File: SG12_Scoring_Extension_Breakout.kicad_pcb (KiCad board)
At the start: 2 copper layers, 95 x 49 mm, 24 parts, among them J1 RJ45, J2 Barrel_Jack_MountingPin, J3 Barrel_Jack_MountingPin, J4 Barrel_Jack_MountingPin, J5 Barrel_Jack_MountingPin, J6 Barrel_Jack_MountingPin, J8 Conn_02x08_Odd_Even, Q1 IRF4905, Q2 IRF4905, Q3 IRF4905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

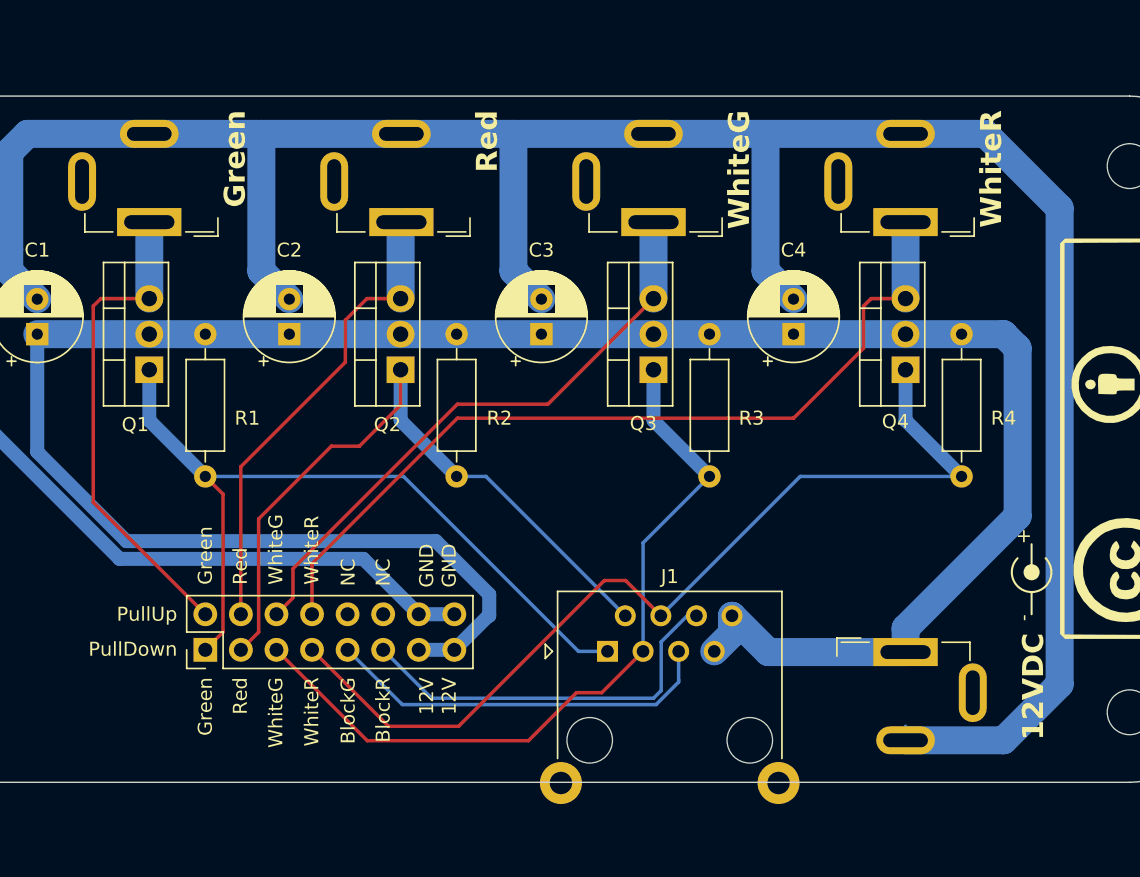
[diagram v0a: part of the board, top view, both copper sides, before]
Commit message: Added 3d models for barrel jacks
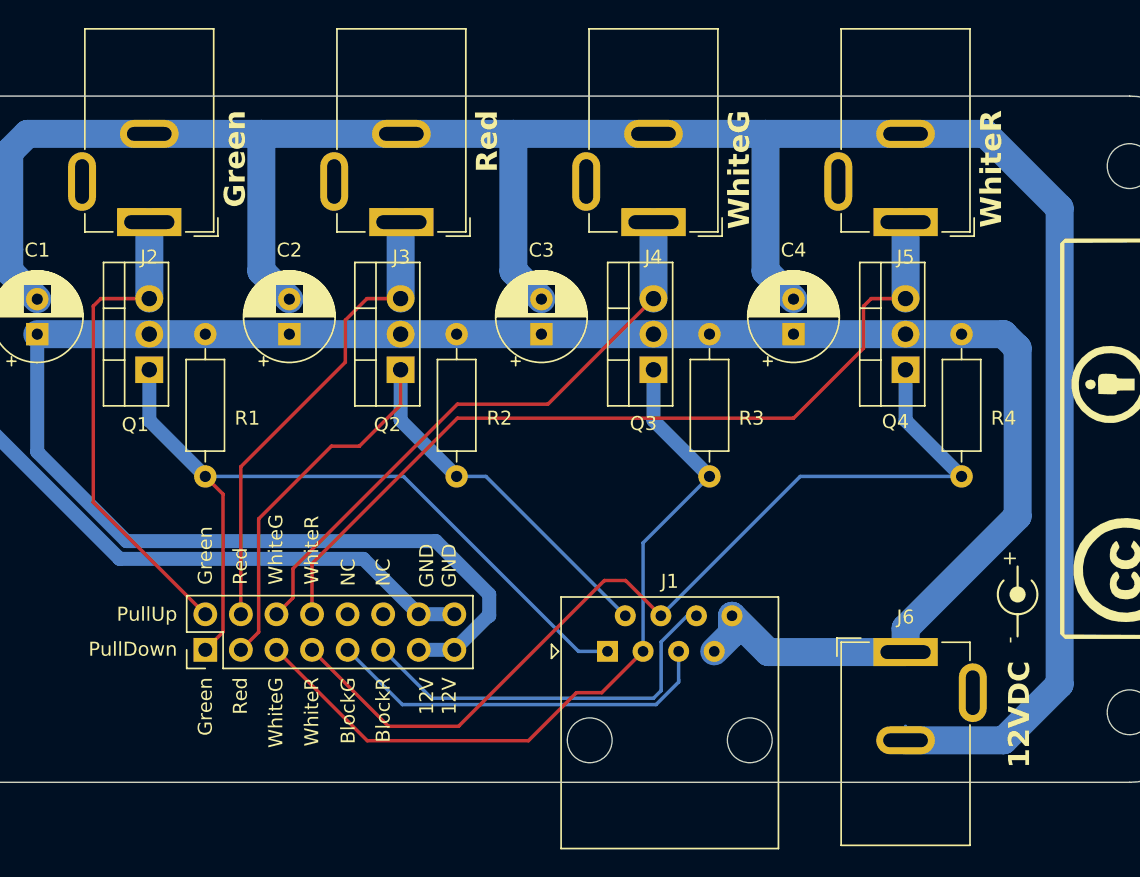
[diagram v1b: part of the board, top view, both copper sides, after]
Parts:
- J1: footprint Connector_RJ:RJ45_Ninigi_GE -> Connector_RJ:RJ45_Amphenol_54602-x08_Horizontal
- J2, J3, J4, J5, J6: footprint Connector_BarrelJack:BarrelJack_GCT_DCJ200-10-A_Horizontal -> Library:BarrelJack_GCT_DCJ200-10-A_Horizontal

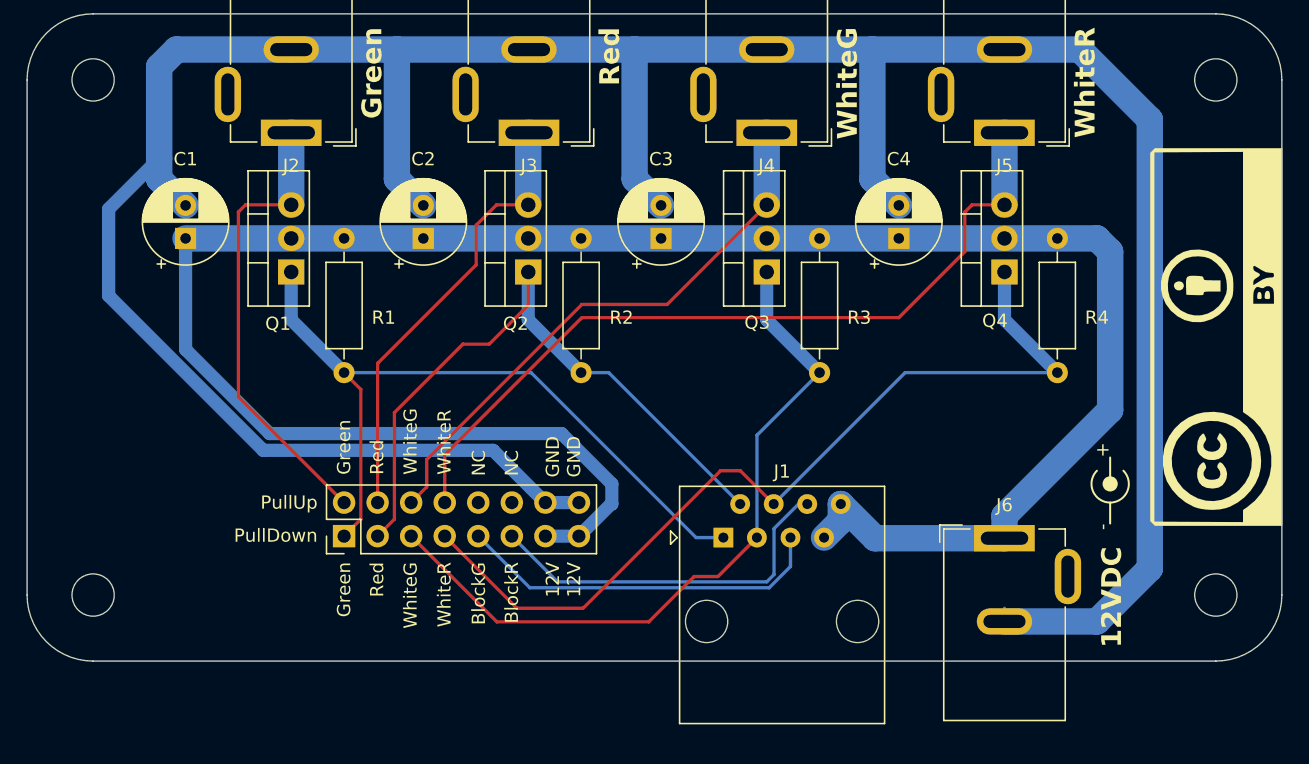
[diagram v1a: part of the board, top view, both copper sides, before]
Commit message: updated pcb dimensions and silkscreen
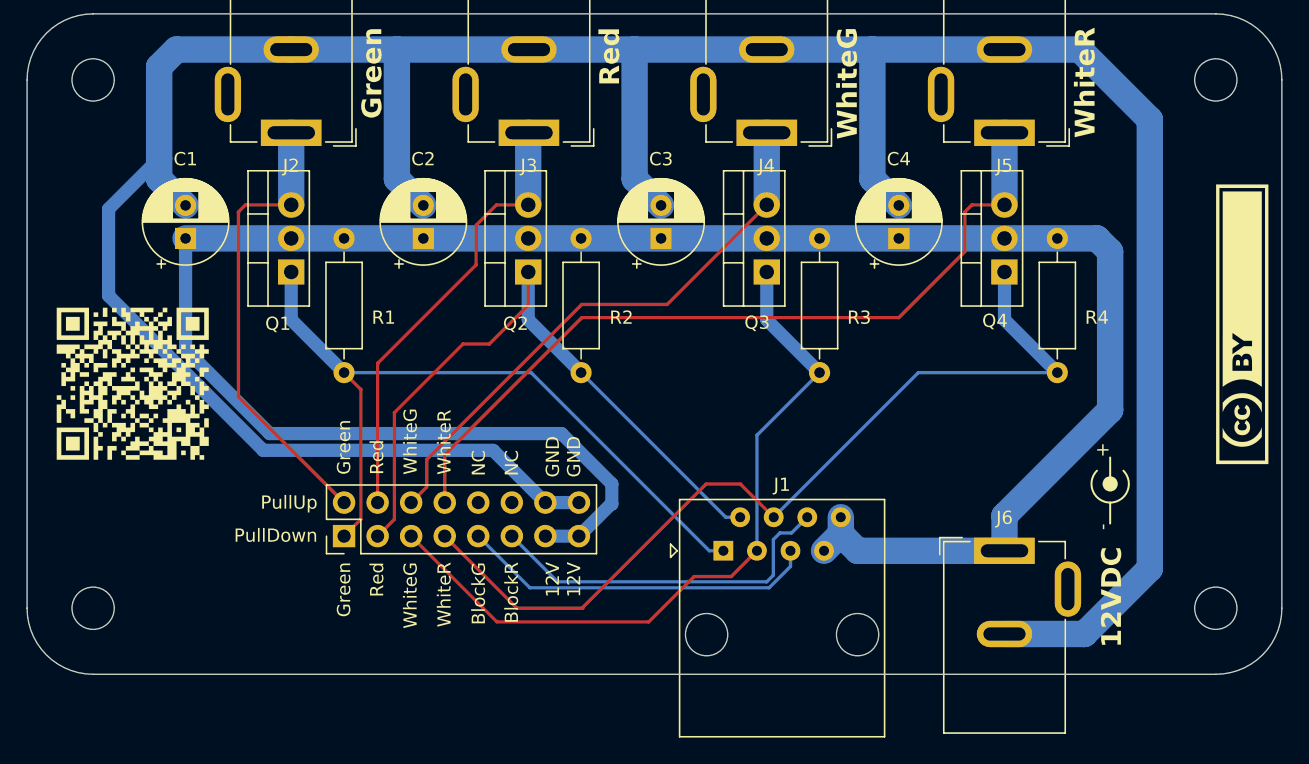
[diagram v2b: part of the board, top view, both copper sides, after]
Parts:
- removed the G*** at (206.0, 105.5)
- added G***: LOGO, LOGO, F.Cu at (124.0, 109.0)
- added G***: LOGO, LOGO, F.Cu at (208.0, 104.5)
- moved J1 1.00 mm to (168.7, 121.7)
- moved REF** 1.00 mm to (121.0, 126.0)
- moved REF** 1.00 mm to (206.0, 126.0)
- moved J6 0.95 mm to (190.0, 121.7)
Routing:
- net Net-(J8-Pin_9): track 28.1 -> 27.1 mm
- net Net-(J8-Pin_11): track 28.3 -> 27.4 mm
- net GND: track 228.7 -> 228.1 mm
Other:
- board size 95 x 49 mm -> 95 x 50 mm

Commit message: various updates
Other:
- board text added: "JLCJLCJLCJLC"

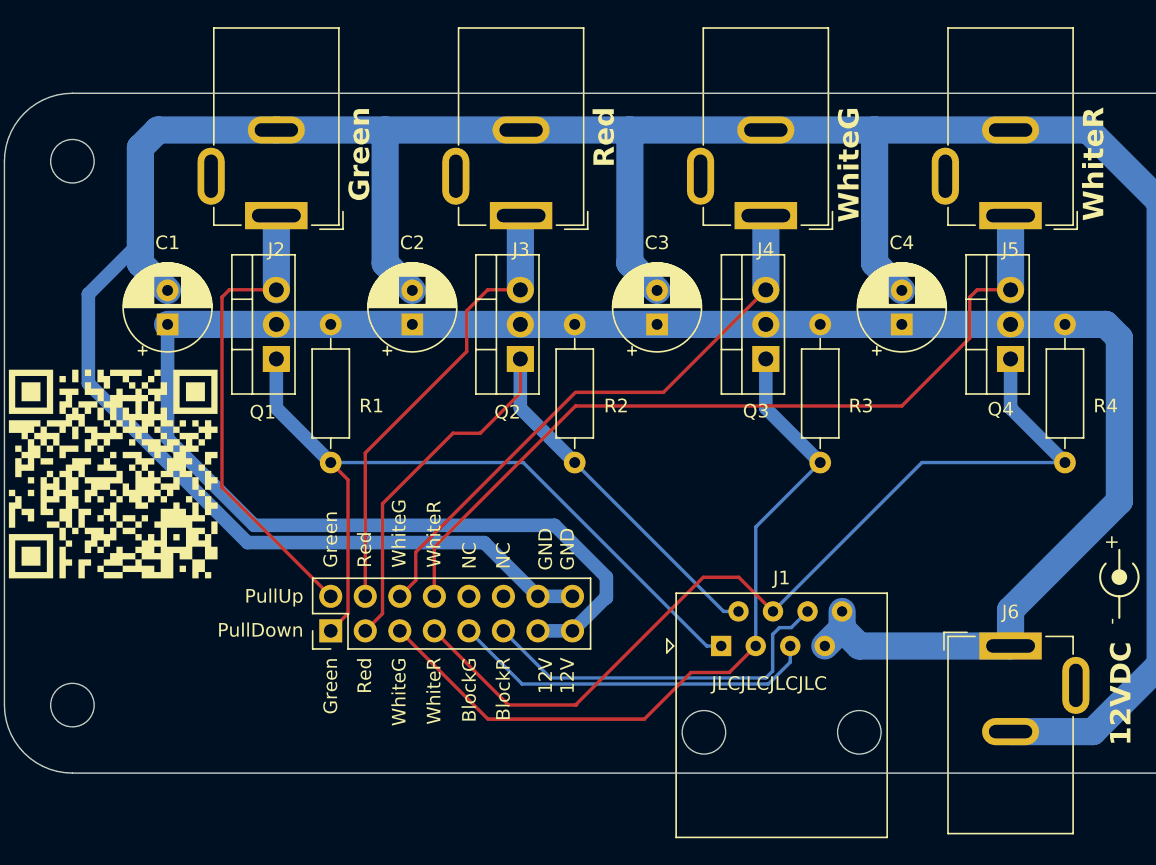
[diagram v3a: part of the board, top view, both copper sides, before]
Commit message: updated some silkscreen and trace widths
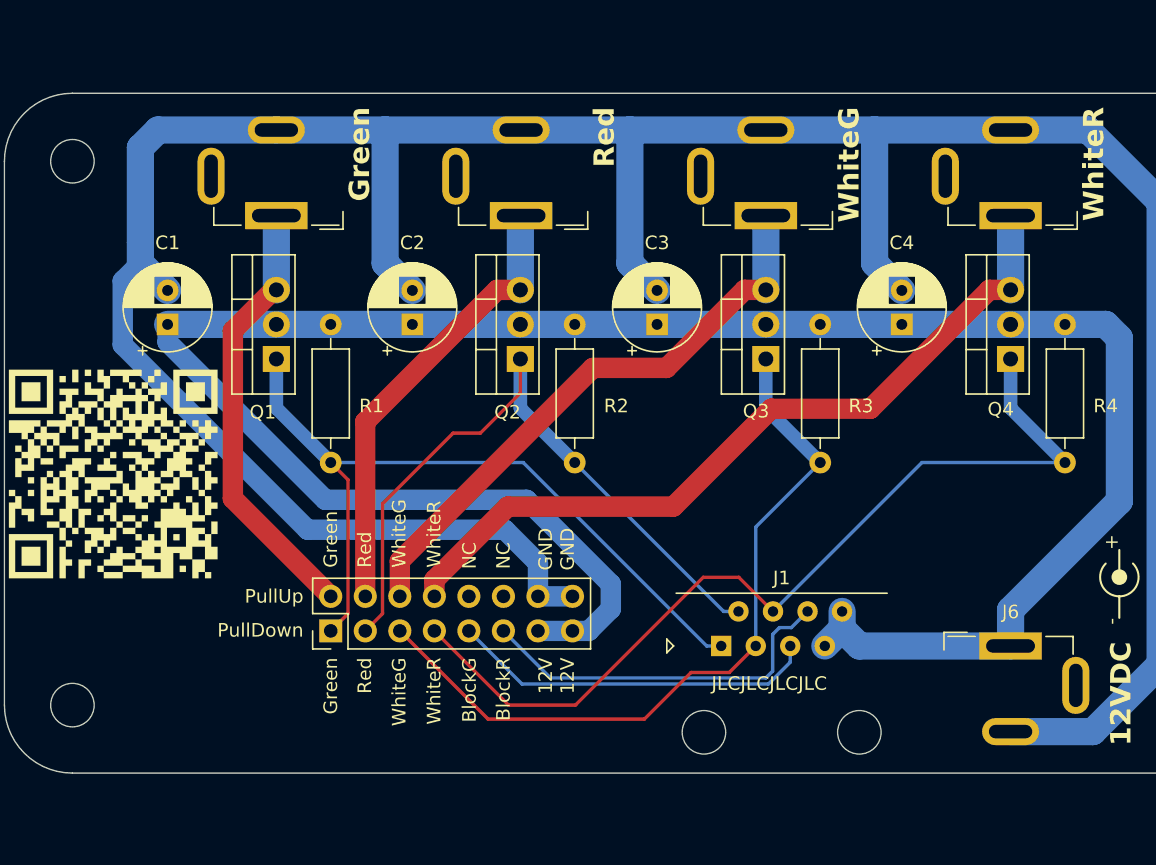
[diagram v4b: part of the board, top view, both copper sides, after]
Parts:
- renumbered G*** to ?
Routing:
- net GND: track 228.1 -> 222.7 mm
- net +12V: track 164.8 -> 161.5 mm
- net /WhiteR_PullUp: track 61.1 -> 57.9 mm
- net /Green_PullUp: track 35.0 -> 32.4 mm

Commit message: Updated schematic with extra connections
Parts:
- removed ?, G***: LOGO, LOGO
- removed C1, C2, C3, C4: C_Polarized, Capacitor_THT:CP_Radial_D6.3mm_P2.50mm
- removed J1: RJ45, Connector_RJ:RJ45_Amphenol_54602-x08_Horizontal
- removed J2, J3, J4, J5, J6: Barrel_Jack_MountingPin, Library:BarrelJack_GCT_DCJ200-10-A_Horizontal
- removed J8: Conn_02x08_Odd_Even, Connector_PinHeader_2.54mm:PinHeader_2x08_P2.54mm_Vertical
- removed Q1, Q2, Q3, Q4: IRF4905, Package_TO_SOT_THT:TO-220-3_Vertical
- removed R1, R2, R3, R4: 10k, Resistor_THT:R_Axial_DIN0207_L6.3mm_D2.5mm_P10.16mm_Horizontal
- removed REF** (x4): MountingHole_3.2mm_M3, MountingHole:MountingHole_3.2mm_M3
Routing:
- net GND: track 222.7 -> 0.00 mm
- net +12V: track 161.5 -> 0.00 mm
- net /WhiteR_PullDown: track 67.4 -> 0.00 mm
- net /WhiteR_PullUp: track 57.9 -> 0.00 mm
- net /Green_PullDown: track 57.0 -> 0.00 mm
- net /WhiteG_PullDown: track 55.8 -> 0.00 mm
- net /Red_PullDown: track 51.8 -> 0.00 mm
- net /WhiteG_PullUp: track 43.2 -> 0.00 mm
- net /Red_PullUp: track 33.7 -> 0.00 mm
- net /Green_PullUp: track 32.4 -> 0.00 mm
- net Net-(J8-Pin_11): track 27.4 -> 0.00 mm
- net Net-(J8-Pin_9): track 27.1 -> 0.00 mm
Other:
- board outline removed
- board text removed: "+"
- board text removed: "-"
- board text removed: "12V 12V"
- board text removed: "12VDC"
- board text removed: "BlockG"
- board text removed: "BlockR"
- board text removed: "GND GND"
- board text removed: "Green"
- board text removed: "JLCJLCJLCJLC"
- board text removed: "NC"
- board text removed: "PullDown"
- board text removed: "PullUp"
- board text removed: "Red"
- board text removed: "WhiteG"
- board text removed: "WhiteR"

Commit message: Rough component placement
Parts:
- added C1: C_Polarized, Capacitor_THT:CP_Radial_D6.3mm_P2.50mm, F.Cu at (132.0, 73.4)
- added C2: C_Polarized, Capacitor_THT:CP_Radial_D6.3mm_P2.50mm, F.Cu at (178.7, 55.3)
- added C3: C_Polarized, Capacitor_THT:CP_Radial_D6.3mm_P2.50mm, F.Cu at (131.5, 97.4)
- added C4: C_Polarized, Capacitor_THT:CP_Radial_D6.3mm_P2.50mm, F.Cu at (169.7, 92.3)
- added C5: C_Polarized, Capacitor_THT:CP_Radial_D6.3mm_P2.50mm, F.Cu at (175.2, 114.3)
- added C6: C_Polarized, Capacitor_THT:CP_Radial_D6.3mm_P2.50mm, F.Cu at (135.5, 128.4)
- added J1: RJ45, Connector_RJ:RJ45_Amphenol_54602-x08_Horizontal, F.Cu at (174.1, 139.2)
- added J10: Conn_01x02, Connector_Phoenix_MSTB:PhoenixContact_MSTBA_2,5_2-G-5,08_1x02_P5.08mm_Horizontal, F.Cu at (107.7, 64.3)
- added J11: Conn_01x02, Connector_Phoenix_MSTB:PhoenixContact_MSTBA_2,5_2-G-5,08_1x02_P5.08mm_Horizontal, F.Cu at (196.9, 63.8)
- added J12: Conn_01x02, Connector_Phoenix_MSTB:PhoenixContact_MSTBA_2,5_2-G-5,08_1x02_P5.08mm_Horizontal, F.Cu at (108.3, 91.9)
- added J13: Conn_01x02, Connector_Phoenix_MSTB:PhoenixContact_MSTBA_2,5_2-G-5,08_1x02_P5.08mm_Horizontal, F.Cu at (196.9, 91.8)
- added J14: Conn_01x02, Connector_Phoenix_MSTB:PhoenixContact_MSTBA_2,5_2-G-5,08_1x02_P5.08mm_Horizontal, F.Cu at (108.3, 118.9)
- added J15: Conn_01x02, Connector_Phoenix_MSTB:PhoenixContact_MSTBA_2,5_2-G-5,08_1x02_P5.08mm_Horizontal, F.Cu at (196.9, 120.8)
- added J16: Conn_02x04_Top_Bottom, Connector_Molex:Molex_Mini-Fit_Jr_5569-08A2_2x04_P4.20mm_Horizontal, F.Cu at (150.1, 57.6)
- added J17: Conn_02x04_Top_Bottom, Connector_Molex:Molex_Mini-Fit_Jr_5569-08A2_2x04_P4.20mm_Horizontal, F.Cu at (129.1, 57.6)
- added J18: Conn_02x04_Top_Bottom, Connector_Molex:Molex_Mini-Fit_Jr_5569-08A2_2x04_P4.20mm_Horizontal, F.Cu at (164.0, 138.0)
- added J19: Conn_01x02, Connector_Phoenix_MSTB:PhoenixContact_MSTBA_2,5_2-G-5,08_1x02_P5.08mm_Horizontal, F.Cu at (137.9, 141.5)
- added J2: Barrel_Jack_MountingPin, Library:BarrelJack_GCT_DCJ200-10-A_Horizontal, F.Cu at (111.8, 79.4)
- added J3: Barrel_Jack_MountingPin, Library:BarrelJack_GCT_DCJ200-10-A_Horizontal, F.Cu at (193.4, 74.3)
- added J4: Barrel_Jack_MountingPin, Library:BarrelJack_GCT_DCJ200-10-A_Horizontal, F.Cu at (111.8, 106.4)
- added J5: Barrel_Jack_MountingPin, Library:BarrelJack_GCT_DCJ200-10-A_Horizontal, F.Cu at (193.3, 102.9)
- added J6: Barrel_Jack_MountingPin, Library:BarrelJack_GCT_DCJ200-10-A_Horizontal, F.Cu at (126.8, 137.9)
- added J7: Barrel_Jack_MountingPin, Library:BarrelJack_GCT_DCJ200-10-A_Horizontal, F.Cu at (111.9, 134.8)
- added J8: Conn_02x08_Odd_Even, Connector_PinHeader_2.54mm:PinHeader_2x08_P2.54mm_Vertical, F.Cu at (148.1, 119.8)
- added J9: Barrel_Jack_MountingPin, Library:BarrelJack_GCT_DCJ200-10-A_Horizontal, F.Cu at (193.3, 131.9)
- added Q1: IRF4905, Package_TO_SOT_THT:TO-220-3_Vertical, F.Cu at (121.0, 81.4)
- added Q2: IRF4905, Package_TO_SOT_THT:TO-220-3_Vertical, F.Cu at (179.2, 75.2)
- added Q3: IRF4905, Package_TO_SOT_THT:TO-220-3_Vertical, F.Cu at (118.3, 102.5)
- added Q4: IRF4905, Package_TO_SOT_THT:TO-220-3_Vertical, F.Cu at (181.9, 101.2)
- added Q5: IRF4905, Package_TO_SOT_THT:TO-220-3_Vertical, F.Cu at (121.8, 130.7)
- added Q6: IRF4905, Package_TO_SOT_THT:TO-220-3_Vertical, F.Cu at (181.2, 129.5)
- added R1: 10k, Resistor_THT:R_Axial_DIN0207_L6.3mm_D2.5mm_P10.16mm_Horizontal, F.Cu at (116.7, 68.7)
- added R2: 10k, Resistor_THT:R_Axial_DIN0207_L6.3mm_D2.5mm_P10.16mm_Horizontal, F.Cu at (176.3, 65.0)
- added R3: 10k, Resistor_THT:R_Axial_DIN0207_L6.3mm_D2.5mm_P10.16mm_Horizontal, F.Cu at (116.4, 94.4)
- added R4: 10k, Resistor_THT:R_Axial_DIN0207_L6.3mm_D2.5mm_P10.16mm_Horizontal, F.Cu at (179.6, 92.3)
- added R5: 10k, Resistor_THT:R_Axial_DIN0207_L6.3mm_D2.5mm_P10.16mm_Horizontal, F.Cu at (119.7, 123.5)
- added R6: 10k, Resistor_THT:R_Axial_DIN0207_L6.3mm_D2.5mm_P10.16mm_Horizontal, F.Cu at (179.6, 120.3)
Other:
- board outline added: 100 x 100 mm
- board text added: "Green"
- board text added: "Red"
